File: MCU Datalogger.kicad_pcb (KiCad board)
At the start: 2 copper layers, 52.1 x 31.8 mm, 30 parts, among them J1 Conn_01x04_Pin, J2 Conn_01x09_Pin, J3 Conn_01x04_Pin, J4 Conn_02x03_Odd_Even, U1 DS1337S_, U2 24LC1025, U3 24LC1025, U4 ATMEGA328P-AU, Y1 32.768 KHz, Y2 16 MHz

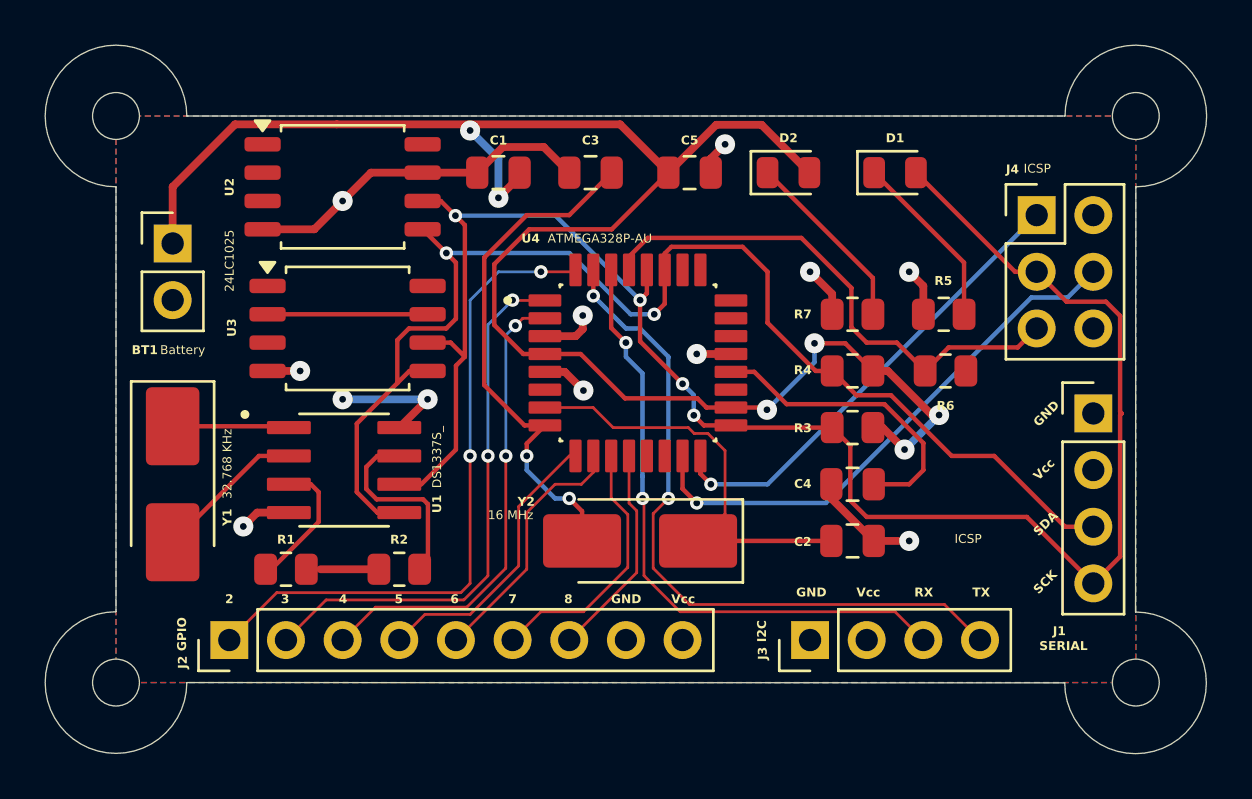
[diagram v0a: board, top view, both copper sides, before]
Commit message: Optimize PCB routing
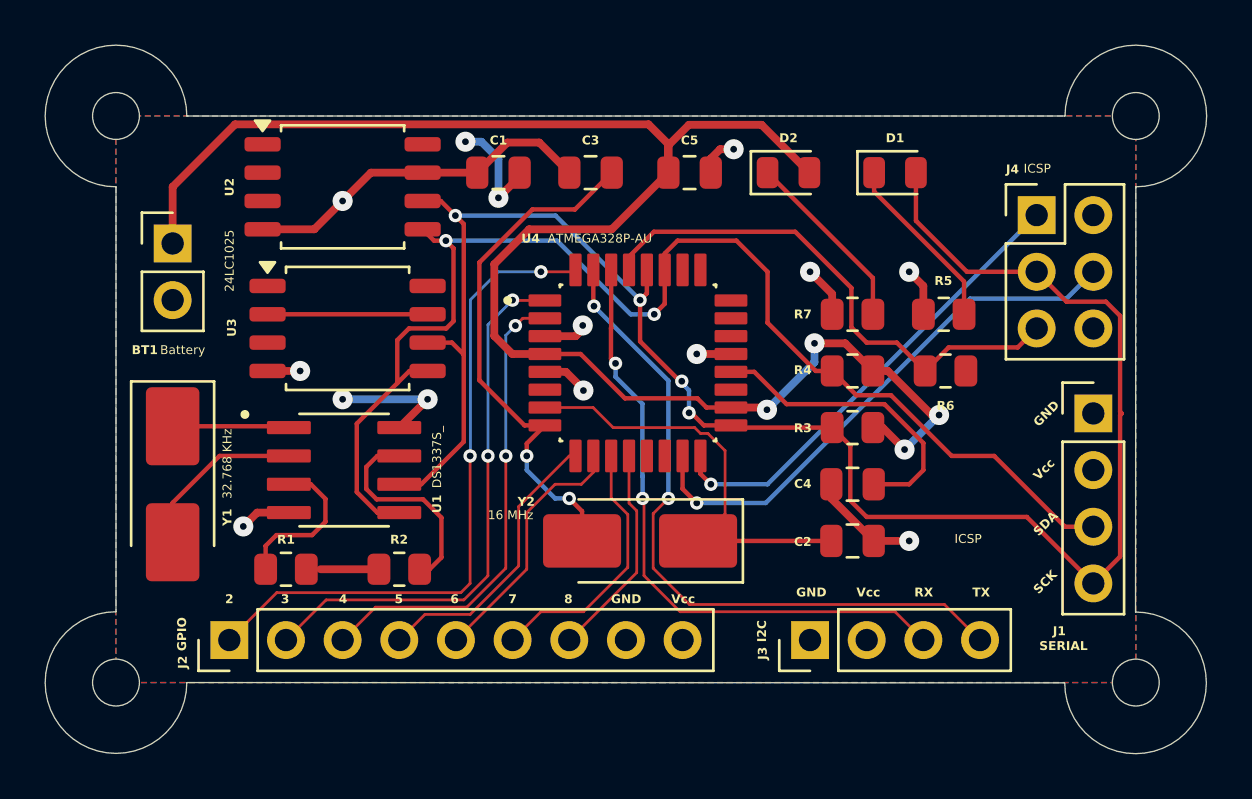
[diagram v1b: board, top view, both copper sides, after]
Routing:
- net /Vcc: track 88.7 -> 90.4 mm
- net /SCK: track 82.0 -> 83.3 mm
- net Net-(U1-~{INTA}): track 6.08 -> 7.11 mm
- net Net-(U1-X2): track 6.81 -> 7.85 mm
- net Net-(U1-SQW/~INT): track 8.79 -> 9.55 mm
- net /SDA: track 58.3 -> 59.0 mm
